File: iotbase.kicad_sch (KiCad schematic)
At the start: 33 parts, among them J1 USB_C_Receptacle_USB2.0, J2 RCWL-0516, SW1 Reset, SW2 Boot, U1 AMS1117-3.3, U2 STF202-22T1G, U3 ESP32-C3-WROOM-02, U4 BME280, U5 GPIO Connector, U6 Connector_ESProg

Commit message: renames symbol and footprint libraries
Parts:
- U2: symbol New_Library:STF202-22T1G -> 0_Project:STF202-22T1G
- U5: footprint 0_my_library:Connector_IoT_GPIO -> 0_Project:Connector_IoT_GPIO; symbol New_Library:Connector_IoT_GPIO -> 0_Project:Connector_IoT_GPIO
- U6: symbol New_Library:Connector_ESProg -> 0_Project:Connector_ESProg
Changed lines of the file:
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@@
     (pin "1")
   )
-  (symbol (lib_id "New_Library:STF202-22T1G") (at 102.87 43.18 0) (unit 1)
+  (symbol (lib_id "0_Project:STF202-22T1G") (at 102.87 43.18 0) (unit 1)
     (in_bom yes) (on_board yes) (fields_autoplaced)
     (property "Reference" "U2" (id 0) (at 102.87 35.052 0))
@@
     (pin "1")
   )
-  (symbol (lib_id "New_Library:Connector_ESProg") (at 274.32 152.4 0) (unit 1)
+  (symbol (lib_id "0_Project:Connector_ESProg") (at 274.32 152.4 0) (unit 1)
     (in_bom yes) (on_board yes) (fields_autoplaced)
     (property "Reference" "U6" (id 0) (at 281.94 161.2899 0)
@@
     (pin "S1")
   )
-  (symbol (lib_id "New_Library:Connector_IoT_GPIO") (at 279.4 109.22 0) (unit 1)
+  (symbol (lib_id "0_Project:Connector_IoT_GPIO") (at 279.4 109.22 0) (unit 1)
     (in_bom no) (on_board yes)
     (property "Reference" "U5" (id 0) (at 285.75 107.9499 0)
@@
       (effects (font (size 1.27 1.27)) (justify left))
     )
-    (property "Footprint" "0_my_library:Connector_IoT_GPIO" (id 2) (at 279.4 87.63 0)
+    (property "Footprint" "0_Project:Connector_IoT_GPIO" (id 2) (at 279.4 87.63 0)
       (effects (font (size 1.27 1.27)) hide)
     )
@@
     )
     (path "/8d61cbc8-355a-4f22-9391-5b6aca3afbe3"
-      (reference "U5") (unit 1) (value "GPIO Connector") (footprint "0_my_library:Connector_IoT_GPIO")
+      (reference "U5") (unit 1) (value "GPIO Connector") (footprint "0_Project:Connector_IoT_GPIO")
     )
     (path "/7ff2b839-3914-4d24-8fd1-3ecdd2bb51fd"

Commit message: updates board layout adds header for RCWL-0516 updates readme
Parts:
- J2: footprint Connector_PinHeader_2.54mm:PinHeader_1x05_P2.54mm_Vertical -> 0_Project:PinHeader_RCWL-0516
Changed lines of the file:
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@@
       (effects (font (size 1.27 1.27)) (justify left))
     )
-    (property "Footprint" "Connector_PinHeader_2.54mm:PinHeader_1x05_P2.54mm_Vertical" (id 2) (at 187.96 180.34 0)
+    (property "Footprint" "0_Project:PinHeader_RCWL-0516" (id 2) (at 187.96 180.34 0)
       (effects (font (size 1.27 1.27)) hide)
     )
@@
     )
     (path "/0fa16a05-7e0d-4f4c-a00e-efd09feb00e1"
-      (reference "J2") (unit 1) (value "RCWL-0516") (footprint "Connector_PinHeader_2.54mm:PinHeader_1x05_P2.54mm_Vertical")
+      (reference "J2") (unit 1) (value "RCWL-0516") (footprint "0_Project:PinHeader_RCWL-0516")
     )
     (path "/9107f90e-86a8-40ce-9b18-211cf27a70d8"

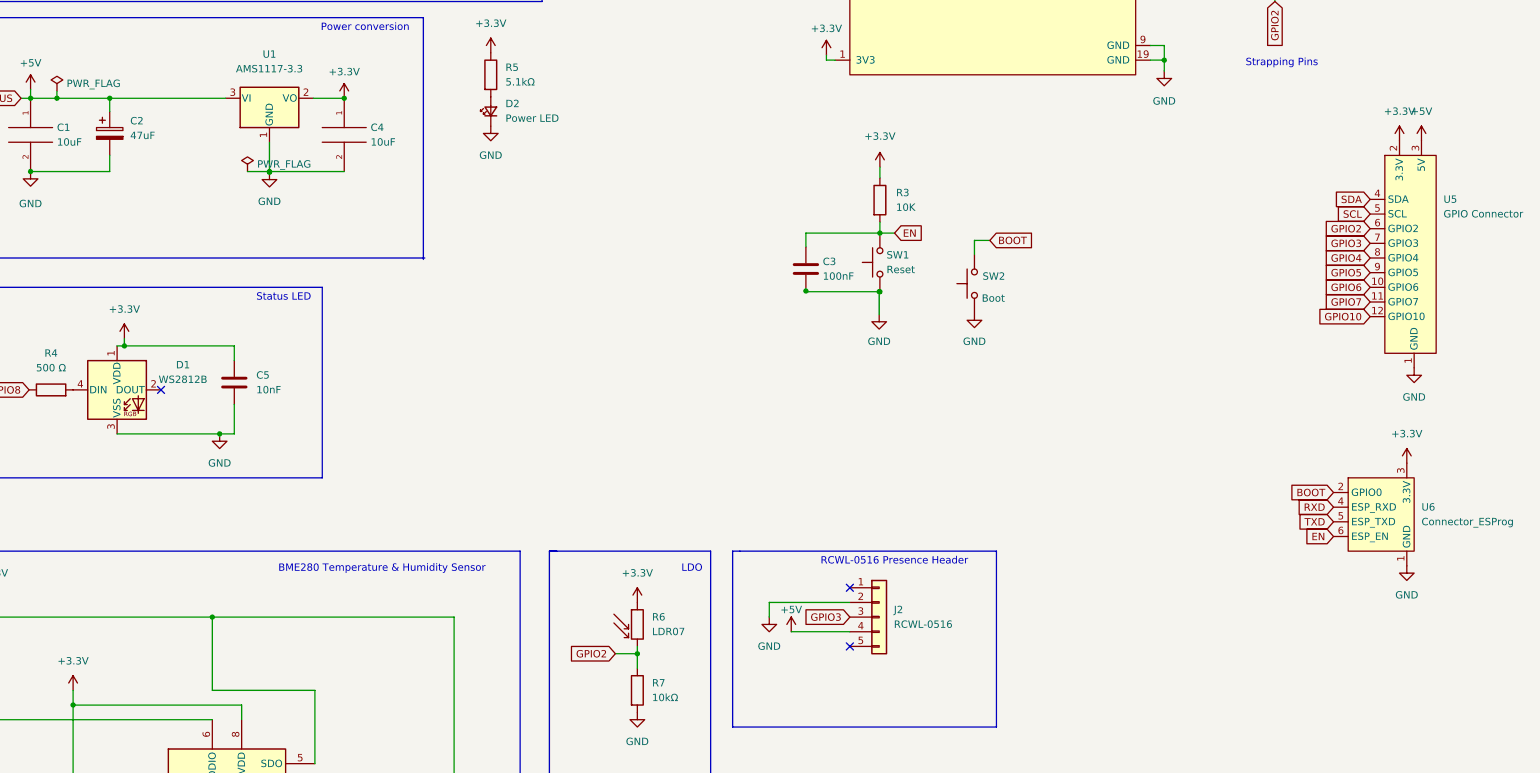
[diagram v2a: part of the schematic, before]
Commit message: updates gpio connector adds additional traces adds jlcpcb fab plugin
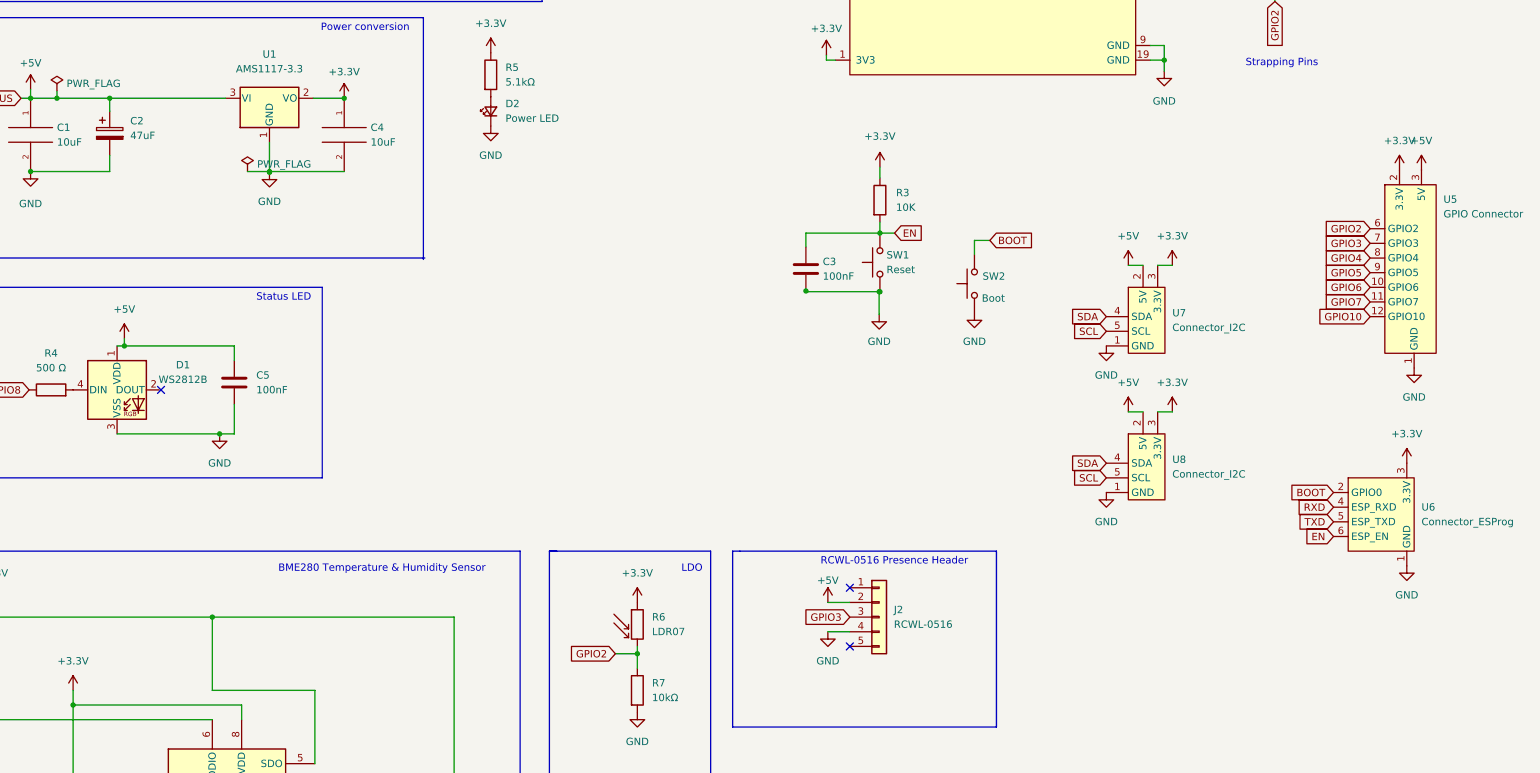
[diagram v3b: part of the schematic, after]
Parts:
- added U7, U8: Connector_I2C, 0_Project:IDC-Header_2x03_P2.54mm_I2C, symbol 0_Project:Connector_I2C
- C2: LCSC part no C96123 -> (none); LSCID (none) -> C96123
- C5: value 10nF -> 100nF
- CB1, CB2: LSCID (none) -> C307331; jlcpcb C307331 -> (none)
- R5: LSCID (none) -> C25905
- RB1, RB2: LSCID (none) -> C25905; jlcpcb C25900 -> (none)
- SW1, SW2: LCSC part no C118141 -> (none); LSCID (none) -> C118141
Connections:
- net +3V3: now also U7.3 (3.3V), U8.3 (3.3V); no longer C5.1, D1.1 (VDD)
- net +5V: now also C5.1, D1.1 (VDD), J2.2 (Pin_2), U7.2 (5V), U8.2 (5V); no longer J2.4 (Pin_4)
- net GND: now also J2.4 (Pin_4), U7.1 (GND), U8.1 (GND); no longer J2.2 (Pin_2)
- net SCL: now also U7.5 (SCL), U8.5 (SCL); no longer U5.5 (SCL)
- net SDA: now also U7.4 (SDA), U8.4 (SDA); no longer U5.4 (SDA)

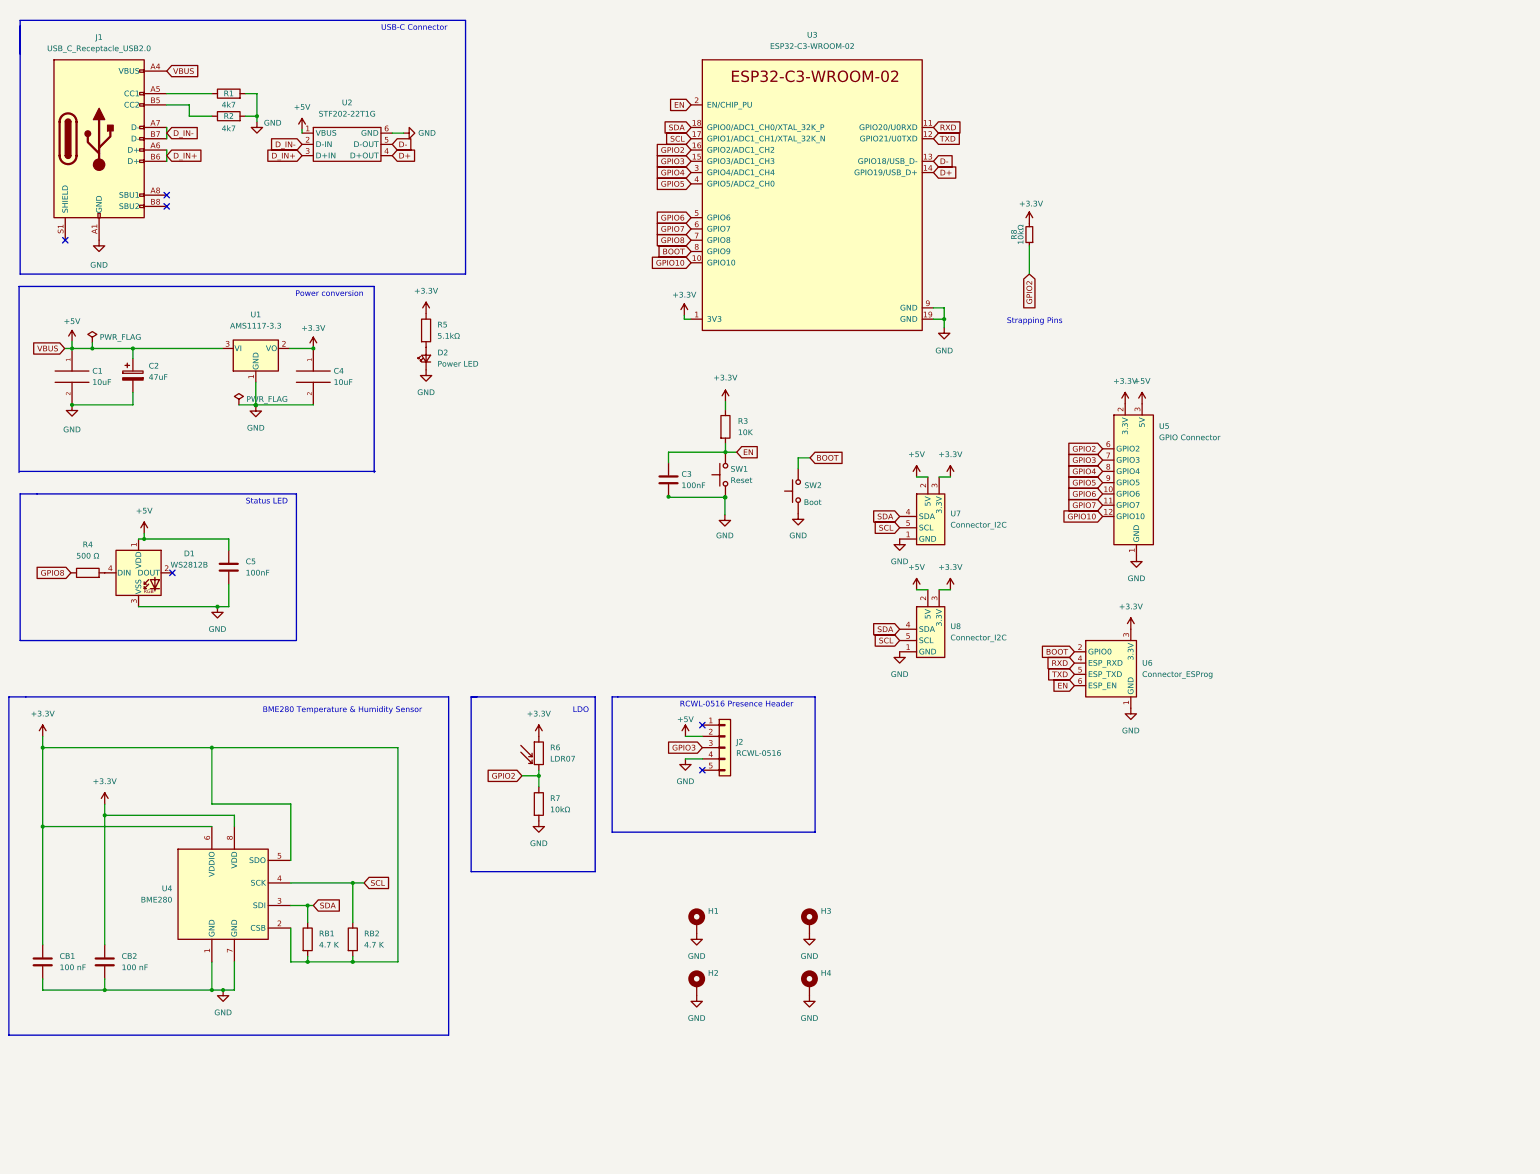
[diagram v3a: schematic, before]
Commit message: updates routes
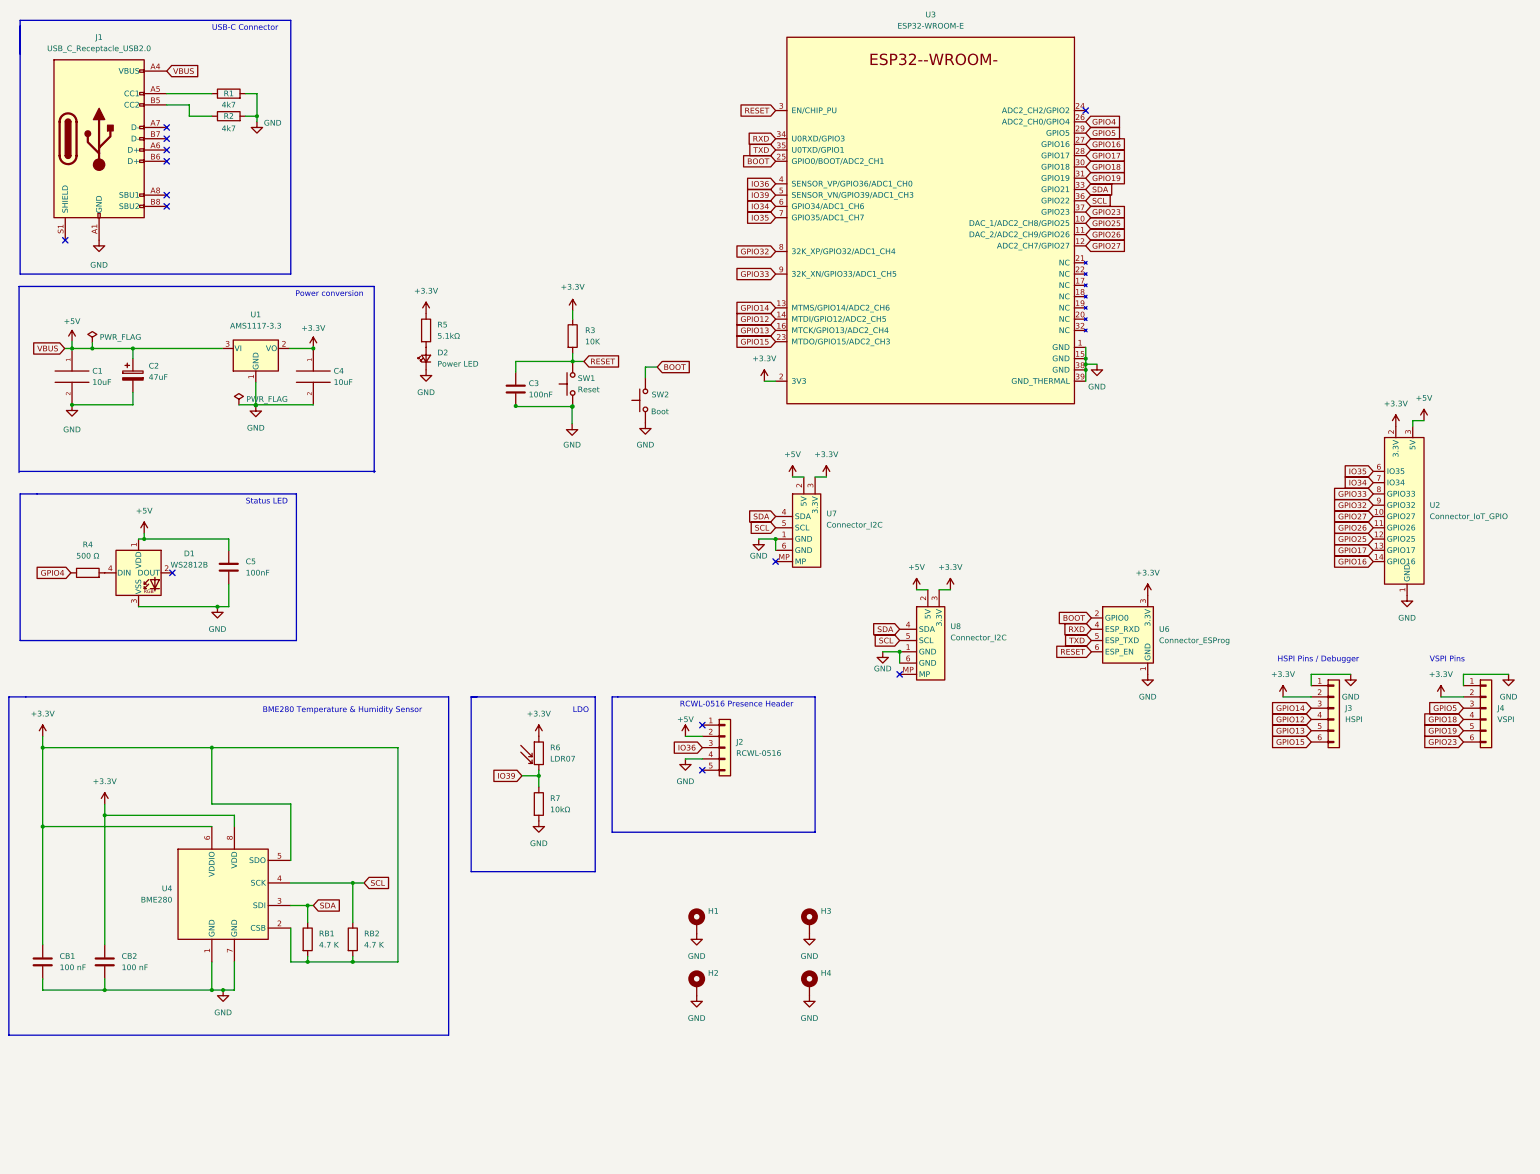
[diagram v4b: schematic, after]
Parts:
- removed R8: 10kΩ, Resistor_SMD:R_0603_1608Metric, symbol Device:R_Small
- removed U2: STF202-22T1G, Package_TO_SOT_SMD:SOT-23-6, symbol 0_Project:STF202-22T1G
- removed U3: ESP32-C3-WROOM-02, Espressif:ESP32-C3-WROOM-02, symbol Espressif:ESP32-C3-WROOM-02
- removed U5: GPIO Connector, 0_Project:Connector_IoT_GPIO, symbol 0_Project:Connector_IoT_GPIO
- added J3: HSPI, Connector_JST:JST_SH_BM06B-SRSS-TB_1x06-1MP_P1.00mm_Vertical, symbol Connector_Generic:Conn_01x06
- added J4: VSPI, Connector_JST:JST_SH_BM06B-SRSS-TB_1x06-1MP_P1.00mm_Vertical, symbol Connector_Generic:Conn_01x06
- added U2: Connector_IoT_GPIO, 0_Project:Connector_IoT_GPIO, symbol 0_Project:Connector_IoT_GPIO
- added U3: ESP32-WROOM-E, Espressif:ESP32-WROOM-32E, symbol Espressif:ESP32-WROOM-E
- U7, U8: footprint 0_Project:IDC-Header_2x03_P2.54mm_I2C -> Connector_JST:JST_SH_BM06B-SRSS-TB_1x06-1MP_P1.00mm_Vertical
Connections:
- net GPIO8 is gone; now on net GPIO4: R4.1
- net +3V3: now also J3.2 (Pin_2), J4.2 (Pin_2), U2.2 (3.3V), U3.2 (3V3)
- net +5V: now also U2.3 (5V)
- net BOOT: now also U3.25 (GPIO0/BOOT/ADC2_CH1)
- net GND: now also U7.6 (GND), U8.6 (GND), J3.1 (Pin_1), J4.1 (Pin_1), U2.1 (GND), U3.1 (GND), U3.15 (GND), U3.38 (GND), U3.39 (GND_THERMAL)
- net GPIO4: now also U3.26 (ADC2_CH0/GPIO4)
- net GPIO5: now also J4.3 (Pin_3), U3.29 (GPIO5)
- net RXD: now also U3.34 (U0RXD/GPIO3)
- net SCL: now also U3.36 (GPIO22)
- net SDA: now also U3.33 (GPIO21)
- net TXD: now also U3.35 (U0TXD/GPIO1)
- net D_IN+: no longer names the net of J1.A6 (D+)
- net D_IN+: no longer J1.B6 (D+)
- net D_IN-: no longer names the net of J1.A7 (D-)
- net D_IN-: no longer J1.B7 (D-)
- net EN renamed RESET
- net RESET: now also U3.3 (EN/CHIP_PU)
- net GPIO2 renamed IO39
- net IO39: now also U3.5 (SENSOR_VN/GPIO39/ADC1_CH3)
- net GPIO3 renamed IO36
- net IO36: now also U3.4 (SENSOR_VP/GPIO36/ADC1_CH0)
- new net GPIO12: J3.4 (Pin_4), U3.14 (MTDI/GPIO12/ADC2_CH5)
- new net GPIO13: J3.5 (Pin_5), U3.16 (MTCK/GPIO13/ADC2_CH4)
- new net GPIO14: J3.3 (Pin_3), U3.13 (MTMS/GPIO14/ADC2_CH6)
- new net GPIO15: J3.6 (Pin_6), U3.23 (MTDO/GPIO15/ADC2_CH3)
- new net GPIO16: U2.14 (GPIO16), U3.27 (GPIO16)
- new net GPIO17: U2.13 (GPIO17), U3.28 (GPIO17)
- new net GPIO18: J4.4 (Pin_4), U3.30 (GPIO18)
- new net GPIO19: J4.5 (Pin_5), U3.31 (GPIO19)
- new net GPIO23: J4.6 (Pin_6), U3.37 (GPIO23)
- new net GPIO25: U2.12 (GPIO25), U3.10 (DAC_1/ADC2_CH8/GPIO25)
- new net GPIO26: U2.11 (GPIO26), U3.11 (DAC_2/ADC2_CH9/GPIO26)
- new net GPIO27: U2.10 (GPIO27), U3.12 (ADC2_CH7/GPIO27)
- new net GPIO32: U2.9 (GPIO32), U3.8 (32K_XP/GPIO32/ADC1_CH4)
- new net GPIO33: U2.8 (GPIO33), U3.9 (32K_XN/GPIO33/ADC1_CH5)
- new net IO34: U2.7 (IO34), U3.6 (GPIO34/ADC1_CH6)
- new net IO35: U2.6 (IO35), U3.7 (GPIO35/ADC1_CH7)
- no-connect marks 6 -> 13
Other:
- note added: "HSPI Pins / Debugger"
- note added: "VSPI Pins"
- note removed: "Strapping Pins"
- moved on the sheet: C3, R3, SW1, SW2, U6

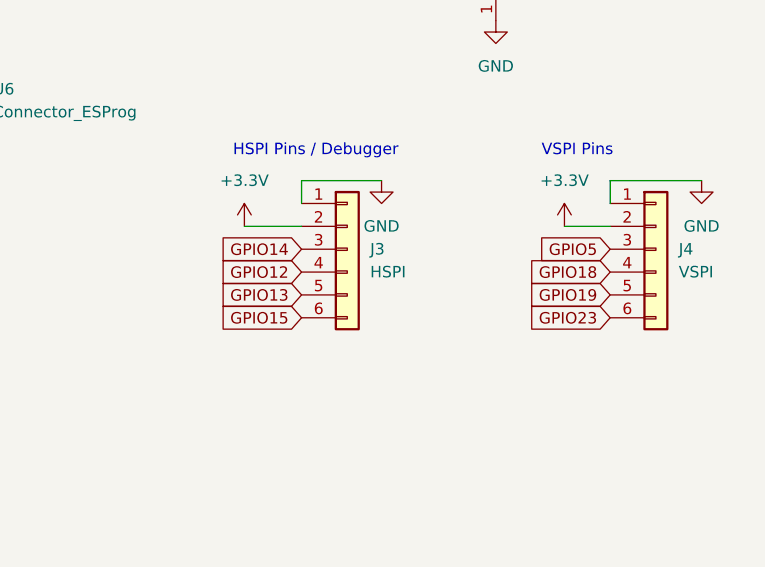
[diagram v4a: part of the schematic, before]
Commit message: updates additional routes
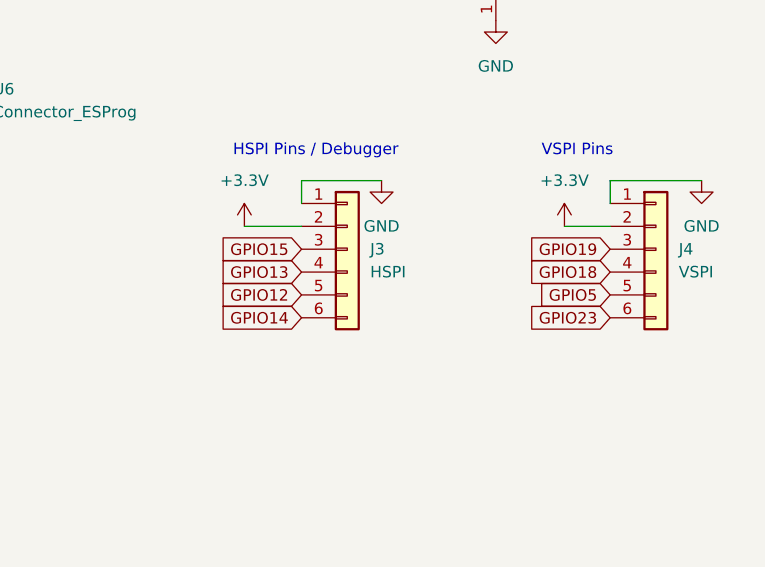
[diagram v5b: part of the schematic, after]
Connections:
- net GPIO12: now also J3.5 (Pin_5); no longer J3.4 (Pin_4)
- net GPIO13: now also J3.4 (Pin_4); no longer J3.5 (Pin_5)
- net GPIO14: now also J3.6 (Pin_6); no longer J3.3 (Pin_3)
- net GPIO15: now also J3.3 (Pin_3); no longer J3.6 (Pin_6)
- net GPIO19: now also J4.3 (Pin_3); no longer J4.5 (Pin_5)
- net GPIO5: now also J4.5 (Pin_5); no longer J4.3 (Pin_3)
